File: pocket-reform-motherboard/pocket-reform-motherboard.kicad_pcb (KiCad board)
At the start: 6 copper layers, 151 x 88 mm, 447 parts, among them J1 CHARGER, J10 1-2199230-6, J11 Conn_01x33, J12 2199230-5, J13 3-2328724-1, J14 USB_C_Receptacle, J15 CONN_SPK, J16 SAMTEC_TSM-106-02-X-SH-A, J17 POWSW, J18 CONN_HEAD, J2 DM3AT-SF-PEJM5, J20 QWIIC, J3 USB_C_Receptacle, J4 09452812561, J5 SYSCTL, J6 USB_INT1, J7 HDMI_D_1.4, J8 SIM_Card, J9 Conn_01x20, SW1 SW_DIP_x01, SW2 RESET, SW3 RESET, U1 reform2-som-connector, U10 W25Q32JVSS, U11 PCF8523T, U12 AP22615AWU-7, U13 TXS0108EPW, U14 SN74AVC1T45, U15 TPD4E02B04DQA, U16 TPD4E02B04DQA, U17 TPD12S521, U18 TLV320AIC3100, U19 TPD4E02B04DQA, U2 TS3USB30EDGSR, U20 TPD4E02B04DQA, U21 TPD4E02B04DQA, U22 TPD4E02B04DQA, U23 FUSB302BMPX, U24 TXS0108EPW, U25 TUSB8041, U26 TPS542021DDC, U27 TVS2200DRV, U28 LM62460, U29 AP22615AWU-7, U3 LM2830XQMFE/NOPB, U30 TS3USB30EDGSR, U31 TS3USB30EDGSR, U32 AP22615AWU-7, U33 AT24CS02-STUM, U34 PCA9536DP, U35 TMUXHS4446RETR, U36 AP22615AWU-7, U37 TS3USB30EDGSR, U38 CY7C65215-32LTXI, U39 PCA9557PW, U4 TLV75718PDBV, U40 AP22615AWU-7, U41 AP22615AWU-7, U5 LM73100RPWR, U6 LM62460, U7 74LVC1G34, U8 RP2040, U9 TPS7A0533PDBZ, Y1 24MHz, Y2 12MHz 12pF, Y3 32.768 kHz

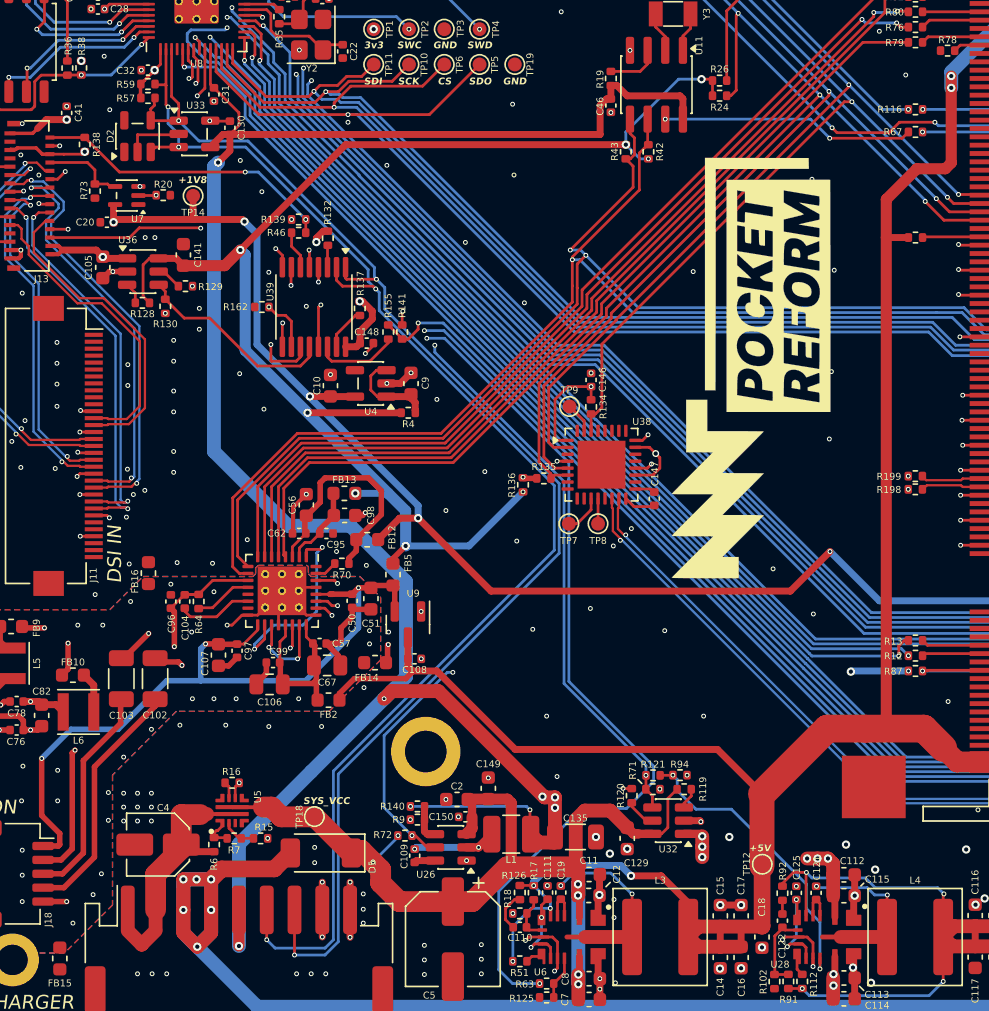
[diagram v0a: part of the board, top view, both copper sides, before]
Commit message: mb2.0 r-1: last minute 3v3 standby dcdc change
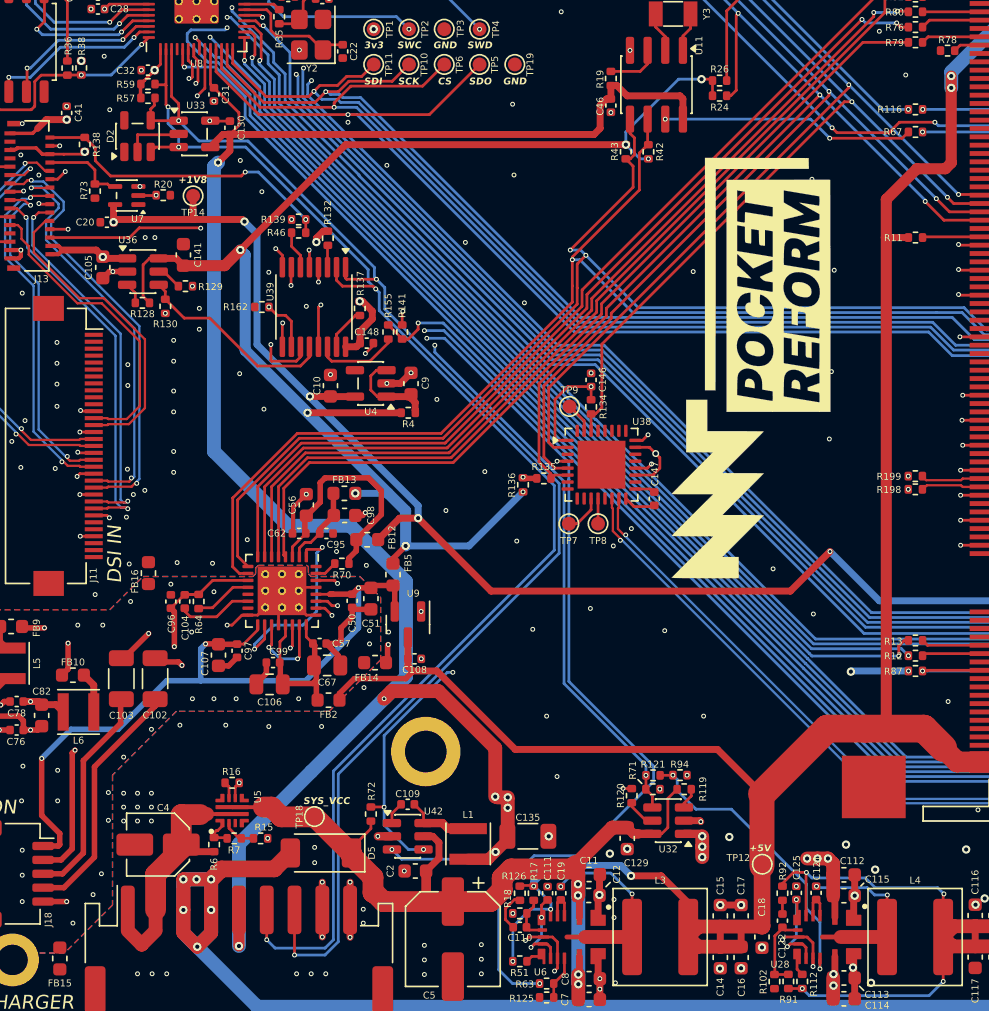
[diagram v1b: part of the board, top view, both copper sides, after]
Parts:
- removed C149: 10uF, Capacitor_SMD:C_0603_1608Metric
- removed C150: 0.1uF, Capacitor_SMD:C_0402_1005Metric
- removed R140: 100k, Resistor_SMD:R_0402_1005Metric
- removed R9: 22k, Resistor_SMD:R_0402_1005Metric
- removed U26: TPS542021DDC, Package_TO_SOT_SMD:SOT-23-6
- added U42: TPS560430X3FDBVR, Package_TO_SOT_SMD:SOT-23-6, F.Cu at (89.5, 140.1)
- L1: value 10uH -> 12uH; footprint Inductor_SMD:L_1210_3225Metric -> Inductor_SMD:L_Taiyo-Yuden_NR-30xx
- R72: value 100k -> 10k
- moved C2 5.96 mm to (90.0, 142.6)
- moved C109 3.73 mm to (89.5, 137.8), turned to 180 degrees
- moved C135 3.43 mm to (98.1, 140.1)
- moved L1 3.18 mm to (93.8, 140.7), turned to -90 degrees
- moved R72 2.90 mm to (86.8, 138.5), turned to 90 degrees
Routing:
- net SYS_VCC: track 71.9 -> 64.9 mm, vias 6 -> 4
- net Net-(U26-FB): track 3.60 -> 0.00 mm
- net Net-(U42-SW): track 6.86 -> 5.00 mm, vias 2 -> 0
- net GND: track 410.9 -> 411.9 mm, vias 638 -> 634
- net ~{STANDBY_SHDN}: track 81.7 -> 82.6 mm, vias 3 -> 4
- net DISP_1EN_2BL: track 21.8 -> 22.6 mm
